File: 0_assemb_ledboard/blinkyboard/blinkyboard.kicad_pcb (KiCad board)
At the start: 2 copper layers, 76.2 x 43.2 mm, 46 parts, among them J1 Conn_01x05, U1 LM2902, U2 LM2902, U3 LM2902, U4 LM2902

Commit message: Add files via upload
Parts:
- R1, R10, R11, R12, R13, R14, R15, R16, R17, R18, R19, R2, R20, R21, R22, R23, R24, R25, R26, R27, R28, R29, R3, R30, R4, R5, R6, R7, R8, R9: moved to F.Cu
- moved R8 121.8 mm to (235.0, 46.1)
- moved R21 107.8 mm to (234.9, 63.9)
- moved R12 104.7 mm to (198.4, 61.5)
- moved R25 101.6 mm to (234.9, 43.6)
- moved R22 98.4 mm to (234.9, 58.9)
- moved R24 97.9 mm to (234.9, 48.6)
- moved R7 97.2 mm to (234.9, 56.3)
- moved R23 96.8 mm to (235.0, 53.7)
- moved R11 95.2 mm to (235.0, 51.2)
- moved R6 89.7 mm to (235.0, 61.3)
- moved R13 83.1 mm to (198.4, 56.1)
- moved R14 81.3 mm to (198.4, 46.2)
- moved R28 81.2 mm to (198.4, 53.8)
- moved R30 81.2 mm to (198.4, 43.4)
- moved R15 78.0 mm to (198.4, 51.3)
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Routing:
- net GND: track 0.00 -> 94.3 mm, vias 0 -> 8
- net OUT_BP: track 0.00 -> 92.9 mm, vias 0 -> 2
- net Comp5: track 0.00 -> 90.9 mm
- net Comp1: track 0.00 -> 86.5 mm
- net Comp4: track 0.00 -> 86.1 mm, vias 0 -> 2
- net Net-(BAR3-Pad1): track 0.00 -> 84.9 mm, vias 0 -> 1
- net Net-(BAR2-Pad5): track 0.00 -> 72.3 mm, vias 0 -> 1
- net OUT_HP: track 0.00 -> 70.8 mm
- net Net-(BAR3-Pad5): track 0.00 -> 62.5 mm
- net Net-(BAR3-Pad7): track 0.00 -> 62.4 mm, vias 0 -> 3
- net Net-(BAR1-Pad5): track 0.00 -> 61.9 mm
- net Comp3: track 0.00 -> 60.0 mm
- net Net-(BAR2-Pad10): track 0.00 -> 59.9 mm, vias 0 -> 1
- net OUT_LP: track 0.00 -> 59.7 mm, vias 0 -> 2
- net Net-(BAR2-Pad7): track 0.00 -> 56.2 mm
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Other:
- board size 76.2 x 43.2 mm -> 95.2 x 46 mm

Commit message: Updates
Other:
- board text added: "5V"
- board text added: "BP"
- board text added: "GND"
- board text added: "HP"
- board text added: "LP"
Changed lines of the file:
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@@
     (property "Sheetname" "")
     (attr smd)
-    (fp_text reference "R8" (at 0 -1.65) (layer "F.SilkS")
+    (fp_text reference "R8" (at -2.794 -1.3412) (layer "F.SilkS")
       (effects (font (size 1 1) (thickness 0.15)))
     )
@@
     (property "Sheetname" "")
     (attr smd)
-    (fp_text reference "R6" (at 0 -1.65) (layer "F.SilkS")
+    (fp_text reference "R6" (at -2.794 -1.3412) (layer "F.SilkS")
       (effects (font (size 1 1) (thickness 0.15)))
     )
@@
     (property "Sheetname" "")
     (attr smd)
-    (fp_text reference "C3" (at 0 -1.68) (layer "F.SilkS")
+    (fp_text reference "C3" (at -2.6416 0) (layer "F.SilkS")
       (effects (font (size 1 1) (thickness 0.15)))
     )
@@
     (property "Sheetname" "")
     (attr smd)
-    (fp_text reference "R17" (at 0 -1.65) (layer "F.SilkS")
+    (fp_text reference "R17" (at -3.004 0.0304) (layer "F.SilkS")
       (effects (font (size 1 1) (thickness 0.15)))
     )
@@
     (property "Sheetname" "")
     (attr smd)
-    (fp_text reference "R11" (at 0 -1.65) (layer "F.SilkS")
+    (fp_text reference "R11" (at -2.794 -1.3412) (layer "F.SilkS")
       (effects (font (size 1 1) (thickness 0.15)))
     )
@@
     (property "Sheetname" "")
     (attr smd)
-    (fp_text reference "C1" (at 0 -1.68) (layer "F.SilkS")
+    (fp_text reference "C1" (at -2.54 -0.2032) (layer "F.SilkS")
       (effects (font (size 1 1) (thickness 0.15)))
     )
@@
     (property "Sheetname" "")
     (attr smd)
-    (fp_text reference "C4" (at 0 -1.68) (layer "F.SilkS")
+    (fp_text reference "C4" (at -2.6416 0) (layer "F.SilkS")
       (effects (font (size 1 1) (thickness 0.15)))
     )
@@
     (property "Sheetname" "")
     (attr smd)
-    (fp_text reference "R5" (at 0 -1.65) (layer "F.SilkS")
+    (fp_text reference "R5" (at -3.004 0.0304) (layer "F.SilkS")
       (effects (font (size 1 1) (thickness 0.15)))
     )
@@
     (property "Sheetname" "")
     (attr smd)
-    (fp_text reference "R12" (at 0 -1.65) (layer "F.SilkS")
+    (fp_text reference "R12" (at -3.1496 0.0508) (layer "F.SilkS")
       (effects (font (size 1 1) (thickness 0.15)))
     )
@@
     (property "Sheetname" "")
     (attr smd)
-    (fp_text reference "R7" (at 0 -1.65) (layer "F.SilkS")
+    (fp_text reference "R7" (at -2.794 -1.3412) (layer "F.SilkS")
       (effects (font (size 1 1) (thickness 0.15)))
     )
@@
     (property "Sheetname" "")
     (attr smd)
-    (fp_text reference "C2" (at 0 -1.68) (layer "F.SilkS")
+    (fp_text reference "C2" (at -2.54 -0.2032) (layer "F.SilkS")
       (effects (font (size 1 1) (thickness 0.15)))
     )
@@
     (property "Sheetname" "")
     (attr smd)
-    (fp_text reference "R1" (at 0 -1.65) (layer "F.SilkS")
+    (fp_text reference "R1" (at -3.004 0.0304) (layer "F.SilkS")
       (effects (font (size 1 1) (thickness 0.15)))
     )
@@
     (property "Sheetname" "")
     (attr smd)
-    (fp_text reference "R22" (at 0 -1.65) (layer "F.SilkS")
+    (fp_text reference "R22" (at -2.794 -1.3412) (layer "F.SilkS")
       (effects (font (size 1 1) (thickness 0.15)))
     )
@@
     (property "Sheetname" "")
     (attr smd)
-    (fp_text reference "R4" (at 0 -1.65) (layer "F.SilkS")
+    (fp_text reference "R4" (at -3.004 0.0304) (layer "F.SilkS")
       (effects (font (size 1 1) (thickness 0.15)))
     )
@@
     (property "Sheetname" "")
     (attr smd)
-    (fp_text reference "R29" (at 0 -1.65) (layer "F.SilkS")
+    (fp_text reference "R29" (at -3.1496 0.0508) (layer "F.SilkS")
       (effects (font (size 1 1) (thickness 0.15)))
     )
@@
     (property "Sheetname" "")
     (attr smd)
-    (fp_text reference "R16" (at 0 -1.65) (layer "F.SilkS")
+    (fp_text reference "R16" (at -3.004 0.0304) (layer "F.SilkS")
       (effects (font (size 1 1) (thickness 0.15)))
     )
@@
     (property "Sheetname" "")
     (attr smd)
-    (fp_text reference "R27" (at 0 -1.65) (layer "F.SilkS")
+    (fp_text reference "R27" (at -3.1496 0.0508) (layer "F.SilkS")
       (effects (font (size 1 1) (thickness 0.15)))
     )
@@
     (property "Sheetname" "")
     (attr smd)
-    (fp_text reference "R9" (at 0 -1.65) (layer "F.SilkS")
+    (fp_text reference "R9" (at -3.1496 0.0508) (layer "F.SilkS")
       (effects (font (size 1 1) (thickness 0.15)))
     )
@@
     (property "Sheetname" "")
     (attr smd)
-    (fp_text reference "R23" (at 0 -1.65) (layer "F.SilkS")
+    (fp_text reference "R23" (at -2.794 -1.3412) (layer "F.SilkS")
       (effects (font (size 1 1) (thickness 0.15)))
     )
@@
     (property "Sheetname" "")
     (attr smd)
-    (fp_text reference "R2" (at 0 -1.65) (layer "F.SilkS")
+    (fp_text reference "R2" (at -2.794 -1.3412) (layer "F.SilkS")
       (effects (font (size 1 1) (thickness 0.15)))
     )
@@
     (property "Sheetname" "")
     (attr smd)
-    (fp_text reference "R14" (at 0 -1.65) (layer "F.SilkS")
+    (fp_text reference "R14" (at -3.1496 0.0508) (layer "F.SilkS")
       (effects (font (size 1 1) (thickness 0.15)))
     )
@@
     (property "Sheetname" "")
     (attr smd)
-    (fp_text reference "R15" (at 0 -1.65) (layer "F.SilkS")
+    (fp_text reference "R15" (at -3.1496 0.0508) (layer "F.SilkS")
       (effects (font (size 1 1) (thickness 0.15)))
     )
@@
     (property "Sheetname" "")
     (attr smd)
-    (fp_text reference "R19" (at 0 -1.65) (layer "F.SilkS")
+    (fp_text reference "R19" (at -3.004 0.0304) (layer "F.SilkS")
       (effects (font (size 1 1) (thickness 0.15)))
     )
@@
     (property "Sheetname" "")
     (attr smd)
-    (fp_text reference "R18" (at 0 -1.65) (layer "F.SilkS")
+    (fp_text reference "R18" (at -3.004 0.0304) (layer "F.SilkS")
       (effects (font (size 1 1) (thickness 0.15)))
     )
@@
     (property "Sheetname" "")
     (attr smd)
-    (fp_text reference "R26" (at 0 -1.65) (layer "F.SilkS")
+    (fp_text reference "R26" (at -2.8956 1.0668) (layer "F.SilkS")
       (effects (font (size 1 1) (thickness 0.15)))
     )
@@
     (property "Sheetname" "")
     (attr smd)
-    (fp_text reference "R3" (at 0 -1.65) (layer "F.SilkS")
+    (fp_text reference "R3" (at -3.004 0.0304) (layer "F.SilkS")
       (effects (font (size 1 1) (thickness 0.15)))
     )
@@
     (property "Sheetname" "")
     (attr smd)
-    (fp_text reference "R24" (at 0 -1.65) (layer "F.SilkS")
+    (fp_text reference "R24" (at -2.794 -1.3412) (layer "F.SilkS")
       (effects (font (size 1 1) (thickness 0.15)))
     )
@@
     (property "Sheetname" "")
     (attr smd)
-    (fp_text reference "R28" (at 0 -1.65) (layer "F.SilkS")
+    (fp_text reference "R28" (at -3.1496 0.0508) (layer "F.SilkS")
       (effects (font (size 1 1) (thickness 0.15)))
     )
@@
     (property "Sheetname" "")
     (attr smd)
-    (fp_text reference "R13" (at 0 -1.65) (layer "F.SilkS")
+    (fp_text reference "R13" (at -3.1496 0.0508) (layer "F.SilkS")
       (effects (font (size 1 1) (thickness 0.15)))
     )
@@
     (property "Sheetname" "")
     (attr smd)
-    (fp_text reference "R20" (at 0 -1.65) (layer "F.SilkS")
+    (fp_text reference "R20" (at -3.004 0.0304) (layer "F.SilkS")
       (effects (font (size 1 1) (thickness 0.15)))
     )
@@
     (property "Sheetname" "")
     (attr smd)
-    (fp_text reference "R21" (at 0 -1.65) (layer "F.SilkS")
+    (fp_text reference "R21" (at -2.794 -1.3412) (layer "F.SilkS")
       (effects (font (size 1 1) (thickness 0.15)))
     )
@@
     (property "Sheetname" "")
     (attr smd)
-    (fp_text reference "R30" (at 0 -1.65) (layer "F.SilkS")
+    (fp_text reference "R30" (at -3.1496 0.0508) (layer "F.SilkS")
       (effects (font (size 1 1) (thickness 0.15)))
     )
@@
     (property "Sheetname" "")
     (attr smd)
-    (fp_text reference "R25" (at 0 -1.65) (layer "F.SilkS")
+    (fp_text reference "R25" (at -2.794 -1.3412) (layer "F.SilkS")
       (effects (font (size 1 1) (thickness 0.15)))
     )
@@
     (property "Sheetname" "")
     (attr smd)
-    (fp_text reference "R10" (at 0 -1.65) (layer "F.SilkS")
+    (fp_text reference "R10" (at -3.0228 0.8432) (layer "F.SilkS")
       (effects (font (size 1 1) (thickness 0.15)))
     )
@@
   )
   (gr_rect (start 144.078 32.009) (end 239.328 77.983) (layer "Edge.Cuts") (width 0.1) (fill none))
+  (gr_text "LP" (at 190.2968 34.6456) (layer "F.SilkS")
+    (effects (font (size 1 1) (thickness 0.15)))
+  )
+  (gr_text "HP" (at 195.3768 34.6456) (layer "F.SilkS")
+    (effects (font (size 1 1) (thickness 0.15)))
+  )
+  (gr_text "BP" (at 192.8368 34.6456) (layer "F.SilkS")
+    (effects (font (size 1 1) (thickness 0.15)))
+  )
+  (gr_text "GND" (at 187.7568 34.6456) (layer "F.SilkS")
+    (effects (font (size 1 1) (thickness 0.15)))
+  )
+  (gr_text "5V" (at 185.166 34.6456) (layer "F.SilkS")
+    (effects (font (size 1 1) (thickness 0.15)))
+  )
   (dimension (type aligned) (layer "Dwgs.User")
     (pts (xy 152.206 32.004) (xy 152.146 77.978))

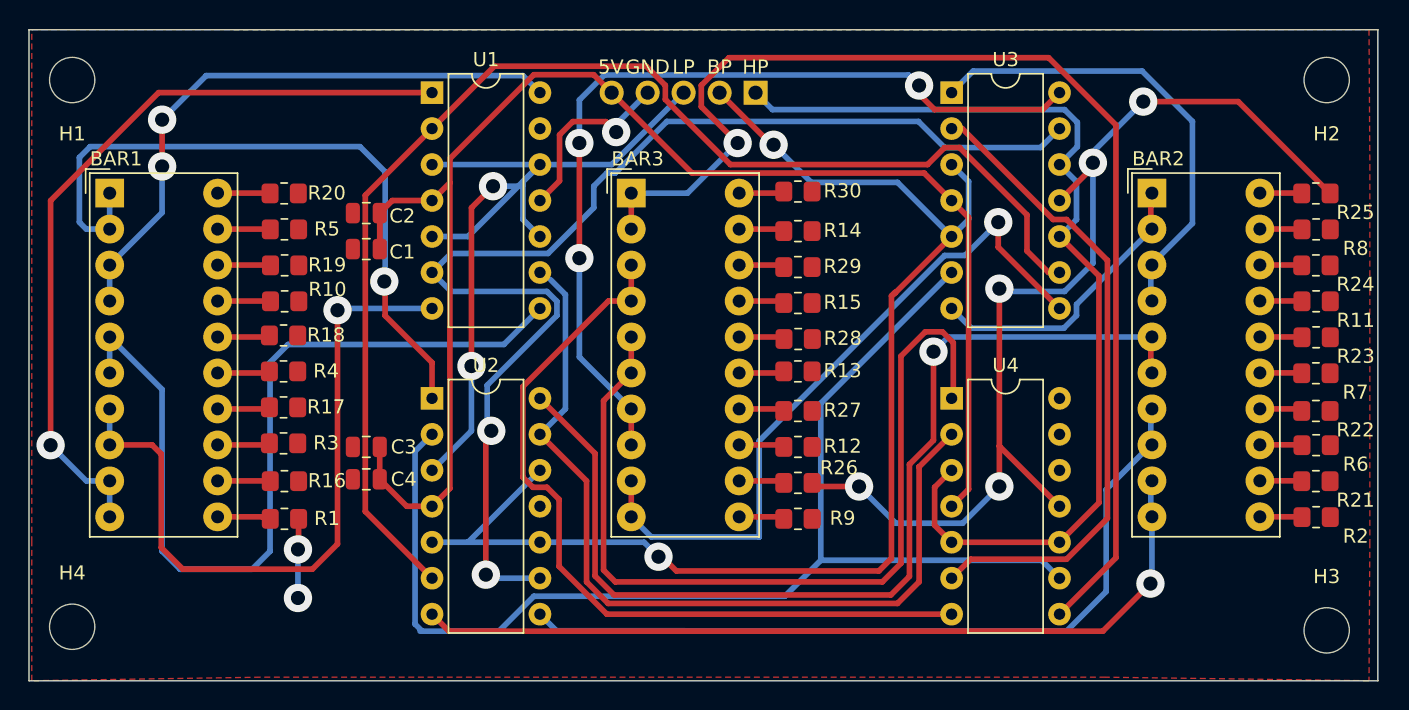
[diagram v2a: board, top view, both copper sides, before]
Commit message: Fixed LED Board and added GND to SPI on Main Board
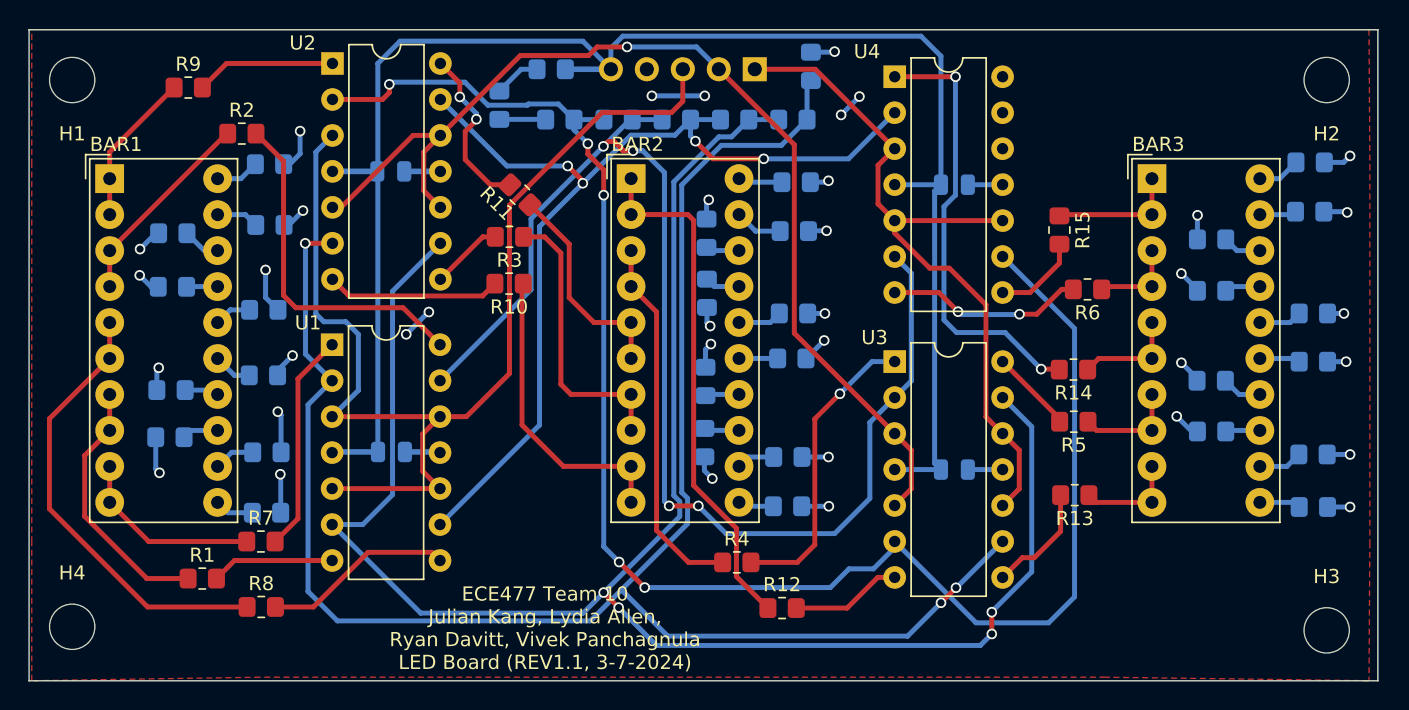
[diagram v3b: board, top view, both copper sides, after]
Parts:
- added R31: 100, Resistor_SMD:R_0805_2012Metric_Pad1.20x1.40mm_HandSolder, B.Cu at (160.9, 61.8)
- added R32: 100, Resistor_SMD:R_0805_2012Metric_Pad1.20x1.40mm_HandSolder, B.Cu at (154.1, 57.5)
- added R33: 100, Resistor_SMD:R_0805_2012Metric_Pad1.20x1.40mm_HandSolder, B.Cu at (160.7, 51.8)
- added R34: 100, Resistor_SMD:R_0805_2012Metric_Pad1.20x1.40mm_HandSolder, B.Cu at (154.2, 46.4)
- added R35: 100, Resistor_SMD:R_0805_2012Metric_Pad1.20x1.40mm_HandSolder, B.Cu at (161.1, 41.5)
- added R36: 100, Resistor_SMD:R_0805_2012Metric_Pad1.20x1.40mm_HandSolder, B.Cu at (197.7, 62.2)
- added R37: 100, Resistor_SMD:R_0805_2012Metric_Pad1.20x1.40mm_HandSolder, B.Cu at (191.8, 56.8)
- added R38: 100, Resistor_SMD:R_0805_2012Metric_Pad1.20x1.40mm_HandSolder, B.Cu at (198.1, 52.0)
- added R39: 100, Resistor_SMD:R_0805_2012Metric_Pad1.20x1.40mm_HandSolder, B.Cu at (191.9, 46.4)
- added R40: 100, Resistor_SMD:R_0805_2012Metric_Pad1.20x1.40mm_HandSolder, B.Cu at (198.2, 42.8)
- added R41: 100, Resistor_SMD:R_0805_2012Metric_Pad1.20x1.40mm_HandSolder, B.Cu at (234.7, 62.0)
- added R42: 100, Resistor_SMD:R_0805_2012Metric_Pad1.20x1.40mm_HandSolder, B.Cu at (227.6, 56.8)
- added R43: 100, Resistor_SMD:R_0805_2012Metric_Pad1.20x1.40mm_HandSolder, B.Cu at (234.8, 52.0)
- added R44: 100, Resistor_SMD:R_0805_2012Metric_Pad1.20x1.40mm_HandSolder, B.Cu at (227.6, 46.8)
- added R45: 100, Resistor_SMD:R_0805_2012Metric_Pad1.20x1.40mm_HandSolder, B.Cu at (234.5, 41.4)
- added R46: 1k, Resistor_SMD:R_0805_2012Metric_Pad1.20x1.40mm_HandSolder, B.Cu at (185.7, 38.4)
- added R47: 1k, Resistor_SMD:R_0805_2012Metric_Pad1.20x1.40mm_HandSolder, B.Cu at (189.8, 38.4)
- added R48: 1k, Resistor_SMD:R_0805_2012Metric_Pad1.20x1.40mm_HandSolder, B.Cu at (193.9, 38.4)
- added R49: 1k, Resistor_SMD:R_0805_2012Metric_Pad1.20x1.40mm_HandSolder, B.Cu at (198.0, 38.4)
- added R50: 1k, Resistor_SMD:R_0805_2012Metric_Pad1.20x1.40mm_HandSolder, B.Cu at (199.3, 34.6)
- added R51: 1k, Resistor_SMD:R_0805_2012Metric_Pad1.20x1.40mm_HandSolder, B.Cu at (180.9, 34.8)
- added R52: 1k, Resistor_SMD:R_0805_2012Metric_Pad1.20x1.40mm_HandSolder, B.Cu at (181.6, 38.4)
- added R53: 1k, Resistor_SMD:R_0805_2012Metric_Pad1.20x1.40mm_HandSolder, B.Cu at (177.3, 37.3)
- C1, C2, C3, C4: moved to B.Cu
- R1, R10, R11, R12, R13, R14, R15, R2, R3, R4, R5, R6, R7, R8, R9: value 150 -> 270
- R16, R17, R18, R19, R20, R21, R22, R23, R24, R25, R26, R27, R28, R29, R30: value 150 -> 100; moved to B.Cu
- moved R25 81.0 mm to (154.2, 50.2), turned to 0 degrees
- moved R2 80.5 mm to (159.1, 39.3), turned to 0 degrees
- moved R8 79.1 mm to (160.5, 72.8), turned to 0 degrees
- moved R7 75.4 mm to (160.5, 68.1), turned to 0 degrees
- moved R5 57.4 mm to (217.9, 59.7)
- moved R11 56.7 mm to (178.7, 43.7), turned to 135 degrees
- moved R9 52.7 mm to (155.3, 36.1), turned to 0 degrees
- moved C4 46.4 mm to (209.4, 43.0), turned to 0 degrees
- moved R21 43.3 mm to (191.8, 61.2), turned to 90 degrees
- moved C3 41.6 mm to (209.4, 63.1), turned to 0 degrees
- moved R23 37.6 mm to (198.1, 46.2)
- moved R22 37.2 mm to (197.9, 55.2)
- moved BAR2 36.8 mm to (186.6, 42.5)
- moved BAR3 36.8 mm to (223.4, 42.5)
- moved R28 36.4 mm to (234.8, 55.4)
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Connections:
- R1 pad 1: GND -> Net-(BAR1-Pad7)
- R1 pad 2: Net-(BAR1-Pad11) -> Net-(R1-Pad2)
- R10 pad 1: GND -> Net-(BAR2-Pad10)
- R10 pad 2: Net-(BAR1-Pad17) -> Net-(R10-Pad2)
- R11 pad 1: GND -> Net-(BAR2-Pad5)
- R11 pad 2: Net-(BAR2-Pad17) -> Net-(R11-Pad2)
- R12 pad 1: GND -> Net-(BAR2-Pad1)
- R12 pad 2: Net-(BAR3-Pad13) -> Net-(R12-Pad2)
- R13 pad 1: GND -> Net-(BAR3-Pad10)
- R13 pad 2: Net-(BAR3-Pad15) -> Net-(R13-Pad2)
- R14 pad 1: GND -> Net-(BAR3-Pad5)
- R14 pad 2: Net-(BAR3-Pad19) -> Net-(R14-Pad2)
- R15 pad 1: GND -> Net-(BAR3-Pad1)
- R15 pad 2: Net-(BAR3-Pad17) -> Net-(R15-Pad2)
- R16 pad 2: Net-(BAR1-Pad12) -> Net-(BAR1-Pad11)
- R17 pad 2: Net-(BAR1-Pad14) -> Net-(BAR2-Pad11)
- R18 pad 2: Net-(BAR1-Pad16) -> Net-(BAR1-Pad13)
- R19 pad 2: Net-(BAR1-Pad18) -> Net-(BAR1-Pad15)
- R2 pad 1: GND -> Net-(BAR1-Pad3)
- R2 pad 2: Net-(BAR2-Pad11) -> Net-(R2-Pad2)
- R20 pad 2: Net-(BAR1-Pad20) -> Net-(BAR1-Pad19)
- R21 pad 2: Net-(BAR2-Pad12) -> Net-(BAR2-Pad13)
- R22 pad 2: Net-(BAR2-Pad14) -> Net-(BAR2-Pad15)
- R23 pad 2: Net-(BAR2-Pad16) -> Net-(BAR2-Pad19)
- R24 pad 2: Net-(BAR2-Pad18) -> Net-(BAR3-Pad11)
- R25 pad 2: Net-(BAR2-Pad20) -> Net-(BAR1-Pad17)
- R26 pad 2: Net-(BAR3-Pad12) -> Net-(BAR2-Pad17)
- R27 pad 2: Net-(BAR3-Pad14) -> Net-(BAR3-Pad13)
- R28 pad 2: Net-(BAR3-Pad16) -> Net-(BAR3-Pad15)
- R29 pad 2: Net-(BAR3-Pad18) -> Net-(BAR3-Pad19)
- R3 pad 1: GND -> Net-(BAR2-Pad7)
- R3 pad 2: Net-(BAR1-Pad13) -> Net-(R3-Pad2)
- R30 pad 2: Net-(BAR3-Pad20) -> Net-(BAR3-Pad17)
- R4 pad 1: GND -> Net-(BAR2-Pad3)
- R4 pad 2: Net-(BAR1-Pad15) -> Net-(R4-Pad2)
- R5 pad 1: GND -> Net-(BAR3-Pad7)
- R5 pad 2: Net-(BAR1-Pad19) -> Net-(R5-Pad2)
- R6 pad 1: GND -> Net-(BAR3-Pad3)
- R6 pad 2: Net-(BAR2-Pad13) -> Net-(R6-Pad2)
- R7 pad 1: GND -> Net-(BAR1-Pad10)
- R7 pad 2: Net-(BAR2-Pad15) -> Net-(R7-Pad2)
- R8 pad 1: GND -> Net-(BAR1-Pad5)
- R8 pad 2: Net-(BAR2-Pad19) -> Net-(R8-Pad2)
- R9 pad 1: GND -> Net-(BAR1-Pad1)
- R9 pad 2: Net-(BAR3-Pad11) -> Net-(R9-Pad2)
- U1 pad 1: Net-(BAR1-Pad10) -> Net-(R7-Pad2)
- U1 pad 13: Comp2 -> Comp4
- U1 pad 14: Net-(BAR1-Pad3) -> Net-(R2-Pad2)
- U1 pad 2: Comp5 -> Comp1
- U1 pad 6: Comp4 -> Comp2
- U1 pad 7: Net-(BAR1-Pad7) -> Net-(R1-Pad2)
- U1 pad 8: Net-(BAR1-Pad5) -> Net-(R8-Pad2)
- U2 pad 1: Net-(BAR1-Pad1) -> Net-(R9-Pad2)
- U2 pad 14: Net-(BAR2-Pad5) -> Net-(R11-Pad2)
- U2 pad 2: Comp1 -> Comp5
- U2 pad 6: Comp5 -> Comp1
- U2 pad 7: Net-(BAR2-Pad10) -> Net-(R10-Pad2)
- U2 pad 8: Net-(BAR2-Pad7) -> Net-(R3-Pad2)
- U2 pad 9: Comp4 -> Comp2
- U3 pad 1: Net-(BAR2-Pad3) -> Net-(R4-Pad2)
- U3 pad 13: Comp4 -> Comp2
- U3 pad 14: Net-(BAR3-Pad7) -> Net-(R5-Pad2)
- U3 pad 2: Comp2 -> Comp4
- U3 pad 6: Comp1 -> Comp5
- U3 pad 7: Net-(BAR2-Pad1) -> Net-(R12-Pad2)
- U3 pad 8: Net-(BAR3-Pad10) -> Net-(R13-Pad2)
- U3 pad 9: Comp5 -> Comp1
- U4 pad 1: Net-(BAR3-Pad5) -> Net-(R14-Pad2)
- U4 pad 6: Comp2 -> Comp4
- U4 pad 7: Net-(BAR3-Pad3) -> Net-(R6-Pad2)
- U4 pad 8: Net-(BAR3-Pad1) -> Net-(R15-Pad2)
- U4 pad 9: Comp1 -> Comp5
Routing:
- net Comp2: track 45.8 -> 135.3 mm, vias 0 -> 4
- net Net-(BAR3-Pad1): track 84.9 -> 8.99 mm, vias 1 -> 0
- net Net-(BAR2-Pad5): track 72.3 -> 15.3 mm, vias 1 -> 0
- net Net-(BAR3-Pad5): track 62.5 -> 7.41 mm
- net Net-(BAR3-Pad7): track 62.4 -> 7.31 mm, vias 3 -> 0
- net Net-(BAR3-Pad3): track 56.1 -> 5.90 mm
- net Net-(BAR3-Pad10): track 50.1 -> 7.20 mm, vias 1 -> 0
- net Net-(BAR1-Pad10): track 55.1 -> 13.4 mm, vias 1 -> 0
- net Comp1: track 86.5 -> 126.9 mm, vias 0 -> 3
- net Net-(BAR1-Pad1): track 49.5 -> 10.9 mm, vias 1 -> 0
- net Net-(BAR2-Pad10): track 59.9 -> 21.3 mm, vias 1 -> 0
- net Net-(BAR2-Pad7): track 56.2 -> 20.2 mm
- net Net-(BAR1-Pad7): track 50.1 -> 18.5 mm, vias 1 -> 0
- net Net-(R14-Pad2): track 0.00 -> 31.4 mm, vias 0 -> 2
- net Net-(BAR1-Pad5): track 61.9 -> 31.7 mm
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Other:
- board text added: "ECE477 Team 10 Julian Kang, Lydia Allen, Ryan Davitt, Vivek Panchagnula LED Board (REV1.1, 3-7-2024)"
